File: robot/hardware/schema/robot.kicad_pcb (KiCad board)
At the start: 2 copper layers, 42 parts, among them P1 CONN_2, P2 CONN_5, P3 CONN_4, P4 CONN_4, P5 CONN_4, P6 CONN_4, SW1 SW_PUSH, SW2 SW_PUSH, U1 74HC595, U10 TB6612FNG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

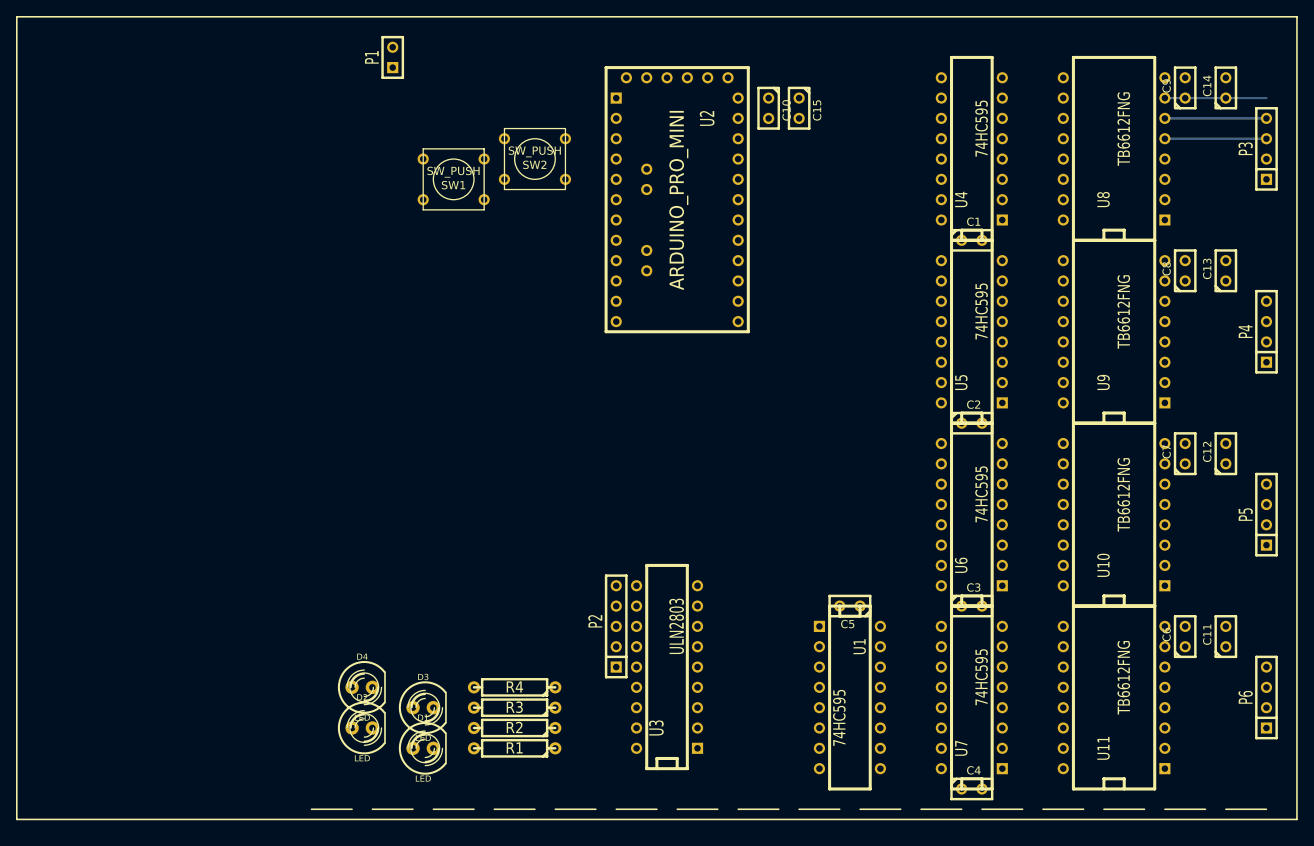
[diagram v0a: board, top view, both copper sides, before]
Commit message: début de connexion. Permutation de l'ordre des registres à décalage
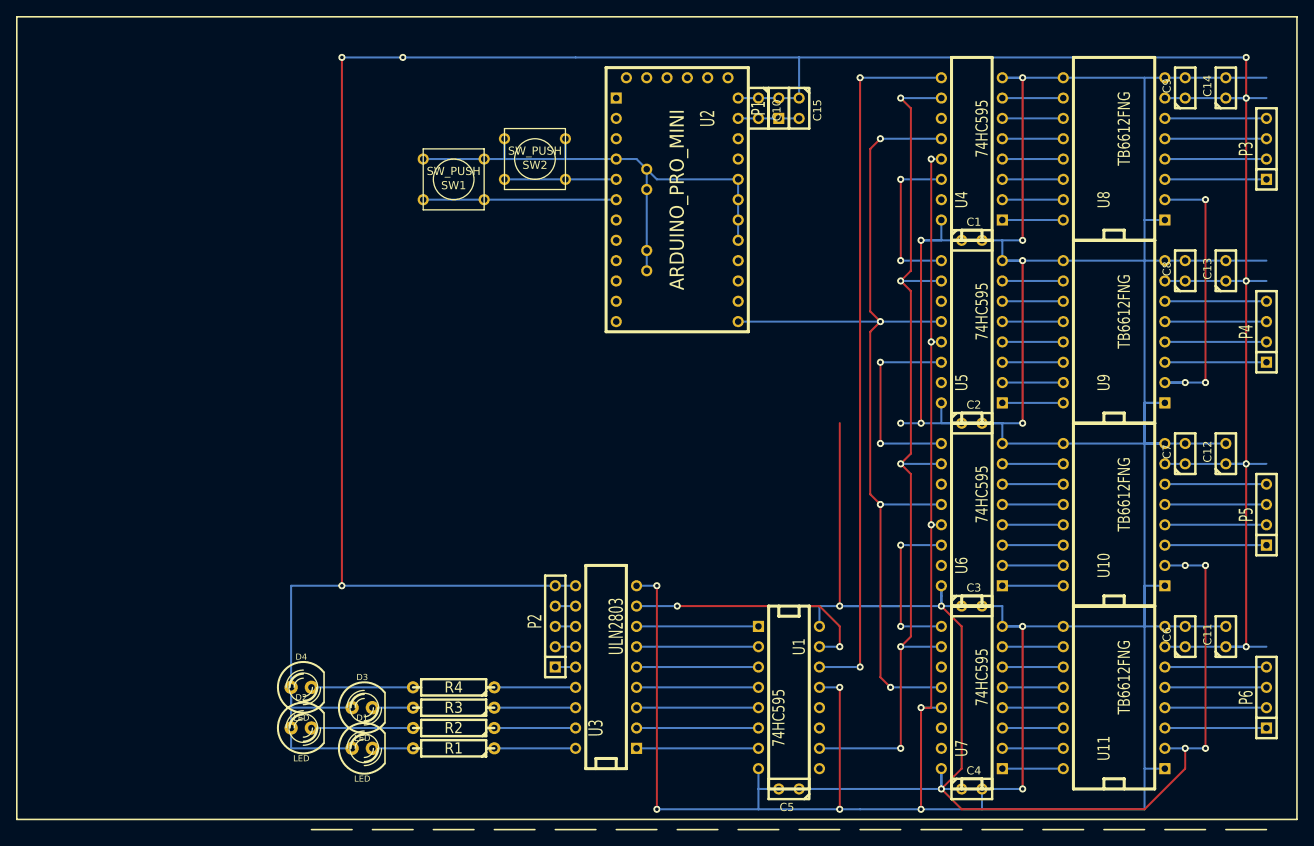
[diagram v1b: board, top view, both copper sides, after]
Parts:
- moved P1 48.7 mm to (108.0, 24.1)
- moved C5 24.1 mm to (109.2, 109.2)
- moved D2 7.62 mm to (48.3, 101.6)
- moved D4 7.62 mm to (48.3, 96.5)
- moved R1 7.62 mm to (67.3, 104.1)
- moved R2 7.62 mm to (67.3, 101.6)
- moved R3 7.62 mm to (67.3, 99.1)
- moved R4 7.62 mm to (67.3, 96.5)
- moved U1 7.62 mm to (109.2, 97.8)
- moved U3 7.62 mm to (86.4, 94.0)
- moved D1 7.62 mm to (55.9, 104.1)
- moved D3 7.62 mm to (55.9, 99.1)
- moved P2 7.62 mm to (80.0, 87.6)
- moved C10 1.27 mm to (105.4, 24.1)
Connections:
- U1 pad 14: N-0000064 (its old number) -> N-0000058
- U2 pad 11A: N-0000095 (its old number) -> N-0000059
- U4 pad 14: N-0000095 (its old number) -> N-0000057
- U4 pad 9: N-0000028 (its old number) -> N-0000058
- U5 pad 14: N-0000028 (its old number) -> N-0000056
- U5 pad 9: N-0000014 (its old number) -> N-0000057
- U6 pad 14: N-0000014 (its old number) -> N-0000061
- U6 pad 9: N-000004 (its old number) -> N-0000056
- U7 pad 14: N-000004 (its old number) -> N-0000059
- U7 pad 9: N-0000064 (its old number) -> N-0000061
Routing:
- net GND: track 0.00 -> 622.1 mm, vias 0 -> 15
- net VMOT: track 12.7 -> 400.0 mm, vias 0 -> 8
- net VCC: track 0.00 -> 261.8 mm, vias 0 -> 13
- net N-0000064: track 0.00 -> 118.2 mm, vias 0 -> 4
- net N-0000091: track 0.00 -> 114.9 mm, vias 0 -> 5
- net N-0000058: track 0.00 -> 88.9 mm, vias 0 -> 2
- net N-0000063: track 0.00 -> 31.5 mm, vias 0 -> 2
- net N-0000056: track 0.00 -> 25.4 mm, vias 0 -> 2
- net N-0000037: track 0.00 -> 24.1 mm
- net N-0000061: track 0.00 -> 20.3 mm, vias 0 -> 2
- net N-0000057: track 0.00 -> 20.3 mm, vias 0 -> 2
- net N-0000062: track 0.00 -> 15.2 mm
- net N-0000032: track 0.00 -> 15.2 mm
- net N-0000031: track 0.00 -> 15.2 mm
- net N-0000025: track 0.00 -> 15.2 mm
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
